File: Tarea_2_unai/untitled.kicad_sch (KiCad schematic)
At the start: 0 parts

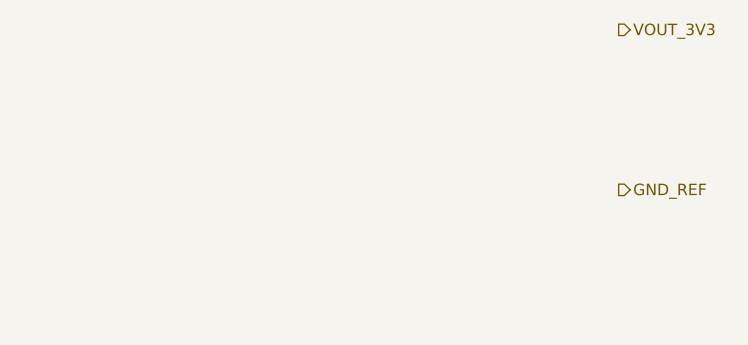
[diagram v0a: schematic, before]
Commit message: cambio de huellas
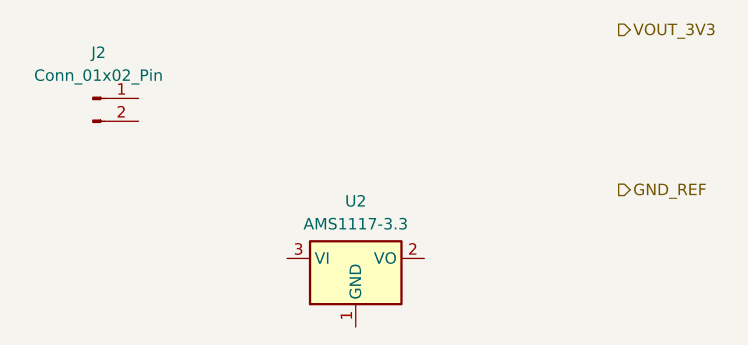
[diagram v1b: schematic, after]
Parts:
- added J2: Conn_01x02_Pin, symbol Connector:Conn_01x02_Pin
- added U2: AMS1117-3.3, Package_TO_SOT_SMD:SOT-223-3_TabPin2, symbol Regulator_Linear:AMS1117-3.3
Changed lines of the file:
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@@
+		)
+	)
+	(symbol
+		(lib_id "Regulator_Linear:AMS1117-3.3")
+		(at 144.78 114.3 0)
+		(unit 1)
+		(body_style 1)
+		(exclude_from_sim no)
+		(in_bom yes)
+		(on_board yes)
+		(in_pos_files yes)
+		(dnp no)
+		(fields_autoplaced yes)
+		(property "Reference" "U2"
+			(at 144.78 107.95 0)
+			(show_name no)
+			(do_not_autoplace no)
+			(effects
+				(font
+					(size 1.27 1.27)
+				)
+			)
+		)
+		(property "Value" "AMS1117-3.3"
+			(at 144.78 110.49 0)
+			(show_name no)
+			(do_not_autoplace no)
+			(effects
+				(font
+					(size 1.27 1.27)
+				)
+			)
+		)
+		(property "Footprint" "Package_TO_SOT_SMD:SOT-223-3_TabPin2"
+			(at 144.78 109.22 0)
+			(hide yes)
+			(show_name no)
+			(do_not_autoplace no)
+			(effects
+				(font
+					(size 1.27 1.27)
+				)
+			)
+		)
+		(property "Datasheet" "http://www.advanced-monolithic.com/pdf/ds1117.pdf"
+			(at 147.32 120.65 0)
+			(hide yes)
+			(show_name no)
+			(do_not_autoplace no)
+			(effects
+				(font
+					(size 1.27 1.27)
+				)
+			)
+		)
+		(property "Description" "1A Low Dropout regulator, positive, 3.3V fixed output, SOT-223"
+			(at 144.78 114.3 0)
+			(hide yes)
+			(show_name no)
+			(do_not_autoplace no)
+			(effects
+				(font
+					(size 1.27 1.27)
+				)
+			)
+		)
+		(pin "1"
+		)
+		(pin "3"
+		)
+		(pin "2"
+		)
+		(instances
+			(project "Tarea_2_unai"
+				(path "/2324ac65-aae7-4e51-a8e4-9d93764ceb90/4db549dd-4991-44c2-b6cf-1bb82ef5f647"
+					(reference "U2")
+					(unit 1)
+				)
+			)
+		)
+	)
+	(symbol
+		(lib_id "Connector:Conn_01x02_Pin")
+		(at 115.57 96.52 0)
+		(unit 1)
+		(body_style 1)
+		(exclude_from_sim no)
+		(in_bom yes)
+		(on_board yes)
+		(in_pos_files yes)
+		(dnp no)
+		(fields_autoplaced yes)
+		(property "Reference" "J2"
+			(at 116.205 91.44 0)
+			(show_name no)
+			(do_not_autoplace no)
+			(effects
+				(font
+					(size 1.27 1.27)
+				)
+			)
+		)
+		(property "Value" "Conn_01x02_Pin"
+			(at 116.205 93.98 0)
+			(show_name no)
+			(do_not_autoplace no)
+			(effects
+				(font
+					(size 1.27 1.27)
+				)
+			)
+		)
+		(property "Footprint" ""
+			(at 115.57 96.52 0)
+			(hide yes)
+			(show_name no)
+			(do_not_autoplace no)
+			(effects
+				(font
+					(size 1.27 1.27)
+				)
+			)
+		)
+		(property "Datasheet" ""
+			(at 115.57 96.52 0)
+			(hide yes)
+			(show_name no)
+			(do_not_autoplace no)
+			(effects
+				(font
+					(size 1.27 1.27)
+				)
+			)
+		)
+		(property "Description" "Generic connector, single row, 01x02, script generated"
+			(at 115.57 96.52 0)
+			(hide yes)
+			(show_name no)
+			(do_not_autoplace no)
+			(effects
+				(font
+					(size 1.27 1.27)
+				)
+			)
+		)
+		(pin "1"
+		)
+		(pin "2"
+		)
+		(instances
+			(project "Tarea_2_unai"
+				(path "/2324ac65-aae7-4e51-a8e4-9d93764ceb90/4db549dd-4991-44c2-b6cf-1bb82ef5f647"
+					(reference "J2")
+					(unit 1)
+				)
+			)
 		)
 	)
